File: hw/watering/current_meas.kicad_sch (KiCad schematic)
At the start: 7 parts, among them U8 MCP6002-xSN

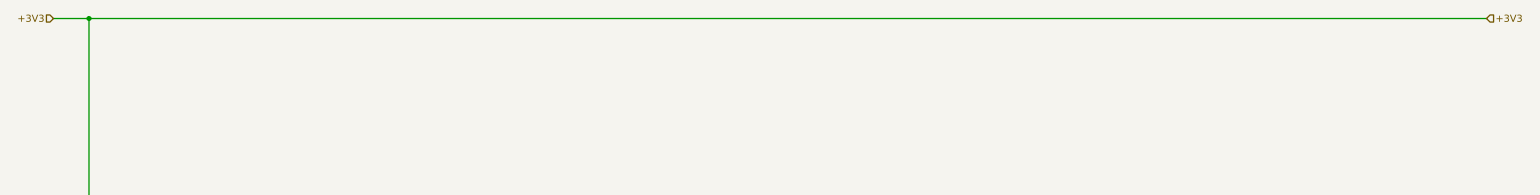
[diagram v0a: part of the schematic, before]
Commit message: connections completet. started placing and routing
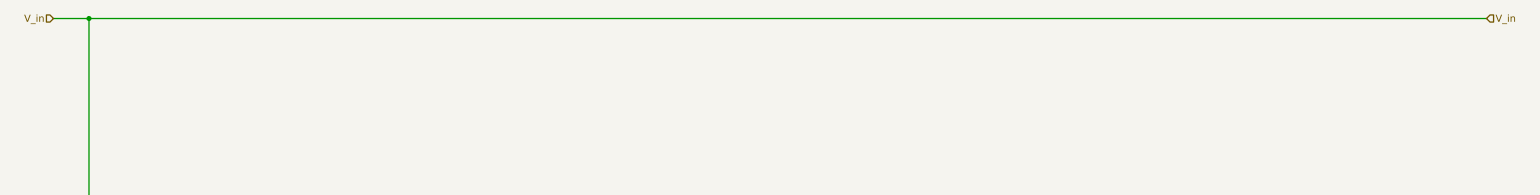
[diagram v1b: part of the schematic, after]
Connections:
- net +3V3 renamed V_in
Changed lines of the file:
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@@
 		)
 	)
-	(hierarchical_label "+3V3"
+	(hierarchical_label "V_in"
 		(shape input)
 		(at 275.59 24.13 0)
@@
 		)
 	)
+	(hierarchical_label "V_in"
+		(shape input)
+		(at 19.05 24.13 180)
+		(effects
+			(font
+				(size 1.27 1.27)
+			)
+			(justify right)
+		)
+	)
 	(hierarchical_label "GND"
 		(shape input)
@@
 		(effects
 			(font
-				(size 1.27 1.27)
-			)
-			(justify right)
-		)
-	)
-	(hierarchical_label "+3V3"
-		(shape input)
-		(at 19.05 24.13 180)
-		(effects
-			(font
